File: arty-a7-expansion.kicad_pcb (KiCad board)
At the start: 4 copper layers, 109.2 x 47 mm, 121 parts, among them IC1 TPD8S009DSMR, IC2 PCA9500PW, J1 SJ-43516-SMT-GR, J2 1140084168, J3 SJ-43516-SMT-BE, J4 685119134923, J5 UE27AC54100, U1 TPS61232DRCT, U2 MAX3421EEHJ, U3 CS4344-CZZ, U4 CS5343-CZZ, U5 NC7SZ126P5X, Y1 ABM8G-12.000MHZ-18-D2Y-T

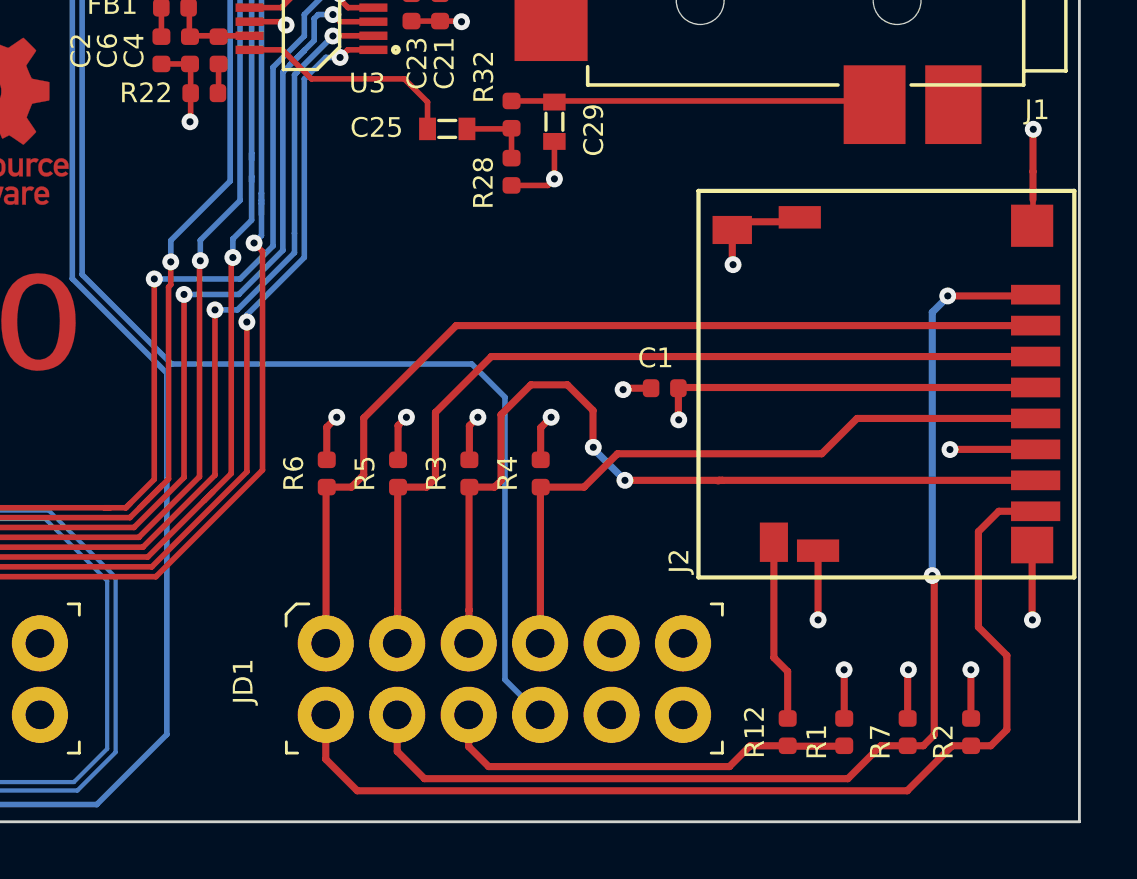
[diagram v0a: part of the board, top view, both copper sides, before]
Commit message: Replace micro SD card connector
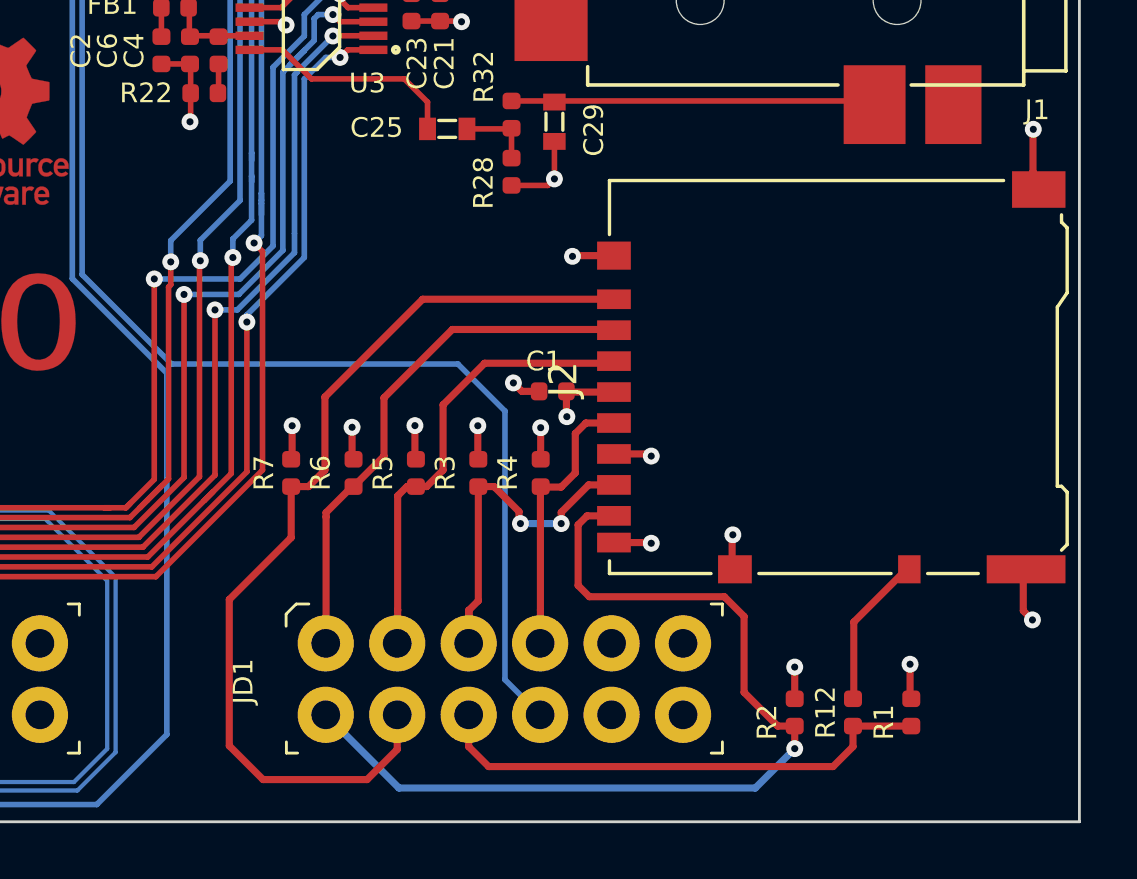
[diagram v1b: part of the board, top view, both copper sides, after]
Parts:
- D7: footprint antmicro-footprints:LED_0603 -> arty-a7-expansion-footprints:LED_0603
- J2: value 1140084168 -> DM3AT-SF-PEJM5; footprint arty-a7-expansion-footprints:MicroSD_1140084168 -> arty-a7-expansion-footprints:MicroSD_DM3AT-SF-PEJM5
- moved R7 23.8 mm to (181.6, 96.9)
- moved R2 6.31 mm to (199.5, 105.4)
- moved C1 3.98 mm to (190.9, 94.0)
- moved R1 2.48 mm to (203.6, 105.4)
- moved R12 2.42 mm to (201.6, 105.4)
- moved J2 1.97 mm to (200.8, 93.5)
- moved R6 0.95 mm to (183.8, 96.9)
- moved R5 0.64 mm to (186.0, 96.9)
- moved R3 0.32 mm to (188.2, 96.9)
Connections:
- J2 pad 10: GND -> Net-(J2-Pad10)
- J2 pad 9: Net-(J2-Pad9) -> GND
- R12 pad 2: Net-(J2-Pad9) -> Net-(J2-Pad10)
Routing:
- net /MISO_DAT0: track 31.0 -> 13.2 mm
- net /CD_DAT3: track 34.3 -> 18.8 mm
- net /MOSI_CMD: track 31.5 -> 16.2 mm
- net +3V3: track 68.0 -> 53.2 mm
- net /SCK: track 24.2 -> 9.85 mm
- net Net-(J2-Pad9): track 6.65 -> 0.00 mm
- net /DAT2: track 40.4 -> 33.9 mm, vias 2 -> 0
- net GND: track 105.4 -> 99.7 mm, vias 50 -> 51
- net Net-(J2-Pad10): track 0.00 -> 5.44 mm
- net /CD: track 15.8 -> 18.9 mm
- net /DAT1: track 37.0 -> 33.9 mm, vias 0 -> 1

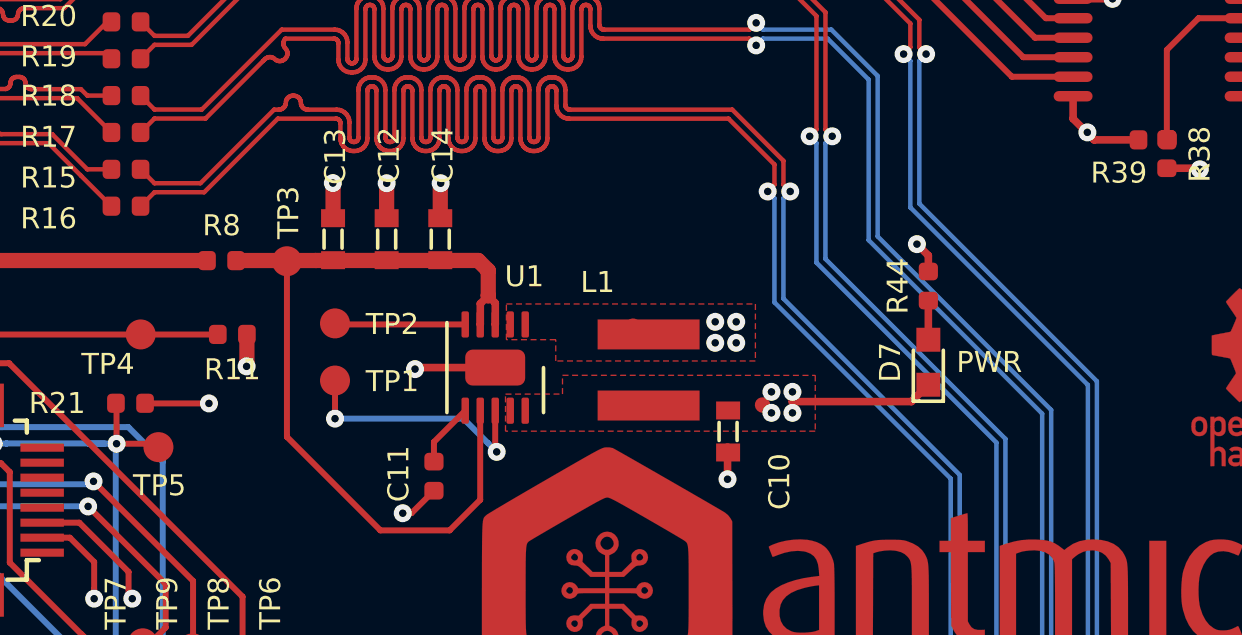
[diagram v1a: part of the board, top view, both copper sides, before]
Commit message: Add 5V0 led indicator
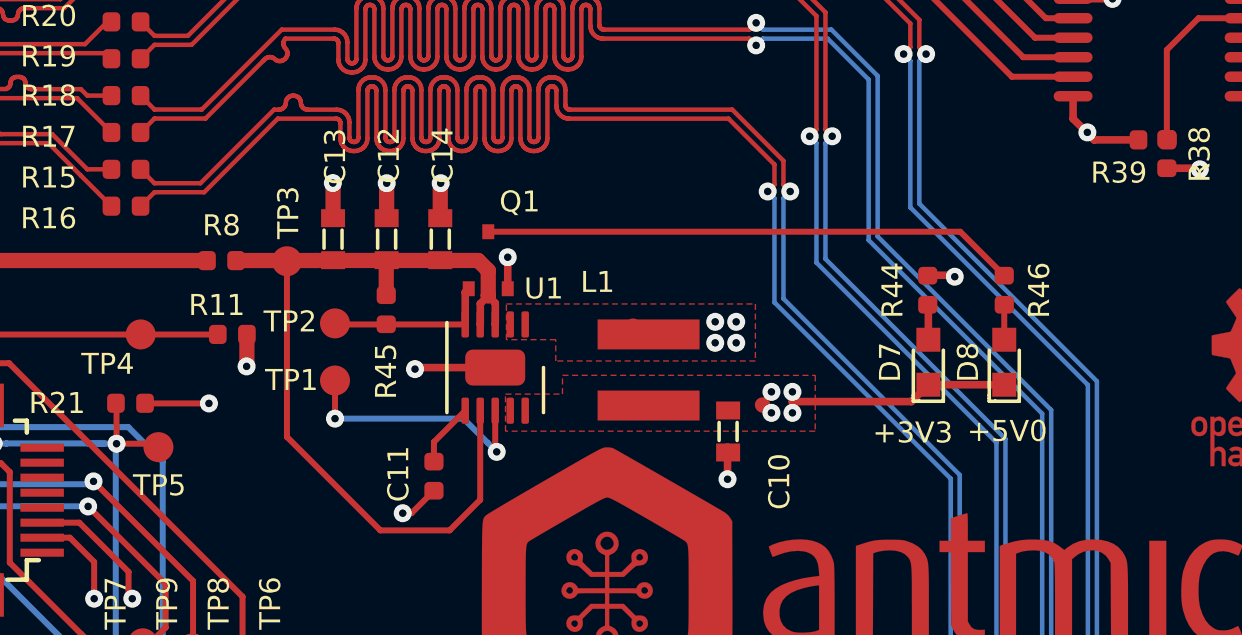
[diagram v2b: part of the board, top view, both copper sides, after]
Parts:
- added D8: LG_L29K-G2J1-24-Z, arty-a7-expansion-footprints:LED_0603, F.Cu at (161.3, 83.9)
- added Q1: BSS138APW, antmicro-footprints:SC70-3, F.Cu at (144.1, 80.5)
- added R45: R_10k_0402, antmicro-footprints:0402-res, F.Cu at (140.7, 82.1)
- added R46: R_330R_0402, antmicro-footprints:0402-res, F.Cu at (161.3, 81.5)
- R44: value R_100R_0402 -> R_330R_0402; footprint arty-a7-expansion-footprints:0402-res -> antmicro-footprints:0402-res
- moved R44 0.14 mm to (158.8, 81.5)
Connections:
- net Net-(C12-Pad1) renamed /5V0
- net Net-(TP2-Pad1) renamed /5V0_PG
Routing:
- net Net-(Q1-Pad3): track 0.00 -> 17.8 mm
- net +3V3: track 53.2 -> 55.8 mm
- net /5V0_PG: track 4.35 -> 5.59 mm
- net /5V0: track 28.5 -> 29.7 mm
- net Net-(D8-Pad2): track 0.00 -> 1.17 mm
- net GND: track 99.7 -> 100.6 mm, vias 51 -> 52
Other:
- board text added: "+3V3"
- board text added: "+5V0"
- board text removed: "PWR"

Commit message: Bump revision to 2.1.0
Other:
- board text added: "Rev.2.1.0 02/2021"
- board text removed: "Rev.2.0.1 07/2020"
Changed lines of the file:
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@@
-(kicad_pcb (version 20171130) (host pcbnew 5.1.6+dfsg1-1~bpo10+1)
+(kicad_pcb (version 20171130) (host pcbnew 5.1.5+dfsg1-2~bpo10+1)
   (general
     (thickness 1.6)
@@
   )
   (setup
-    (last_trace_width 0.508)
+    (last_trace_width 0.254)
     (user_trace_width 0.2)
     (user_trace_width 0.508)
@@
     (effects (font (size 1 1) (thickness 0.25)) (justify left))
   )
-  (gr_text "Rev.2.0.1 07/2020" (at 153.95 96.9385) (layer F.Mask)
+  (gr_text "Rev.2.1.0 02/2021" (at 153.95 96.9385) (layer F.Mask)
     (effects (font (size 1 1) (thickness 0.2)) (justify left))
   )
-  (gr_text "Rev.2.0.1 07/2020" (at 153.95 96.9385) (layer F.Cu)
+  (gr_text "Rev.2.1.0 02/2021" (at 153.95 96.9385) (layer F.Cu)
     (effects (font (size 1 1) (thickness 0.2)) (justify left))
   )
@@
   (segment (start 187.901241 101.773709) (end 187.911241 101.763709) (width 0.254) (layer F.Cu) (net 25))
   (segment (start 187.901241 102.943709) (end 187.901241 101.773709) (width 0.254) (layer F.Cu) (net 25))
-  (segment (start 137.431241 86.374711) (end 137.431241 80.495209) (width 0.2) (layer F.Cu) (net 124))
-  (segment (start 140.54724 89.49071) (end 137.431241 86.374711) (width 0.2) (layer F.Cu) (net 124))
-  (segment (start 142.85424 89.49071) (end 140.54724 89.49071) (width 0.2) (layer F.Cu) (net 124))
-  (segment (start 143.873241 85.501209) (end 143.873241 88.471709) (width 0.2) (layer F.Cu) (net 124))
-  (segment (start 143.873241 88.471709) (end 142.85424 89.49071) (width 0.2) (layer F.Cu) (net 124))
-  (segment (start 138.391241 80.493709) (end 143.806241 80.493709) (width 0.508) (layer F.Cu) (net 124))
-  (segment (start 137.431241 80.495209) (end 138.389741 80.495209) (width 0.508) (layer F.Cu) (net 124))
-  (segment (start 143.806241 80.493709) (end 144.141241 80.828709) (width 0.508) (layer F.Cu) (net 124))
-  (segment (start 138.389741 80.495209) (end 138.391241 80.493709) (width 0.508) (layer F.Cu) (net 124))
-  (segment (start 144.136241 81.673709) (end 144.376241 81.913709) (width 0.254) (layer F.Cu) (net 124))
-  (segment (start 143.876241 81.933709) (end 144.136241 81.673709) (width 0.254) (layer F.Cu) (net 124))
-  (segment (start 144.376241 81.913709) (end 144.376241 82.623209) (width 0.254) (layer F.Cu) (net 124))
-  (segment (start 143.873241 82.626209) (end 143.876241 82.623209) (width 0.254) (layer F.Cu) (net 124))
-  (segment (start 144.376241 82.623209) (end 144.373241 82.626209) (width 0.254) (layer F.Cu) (net 124))
-  (segment (start 143.876241 82.623209) (end 143.876241 81.933709) (width 0.254) (layer F.Cu) (net 124))
-  (segment (start 144.141241 81.668709) (end 144.136241 81.673709) (width 0.508) (layer F.Cu) (net 124))
-  (segment (start 144.141241 80.828709) (end 144.141241 81.668709) (width 0.508) (layer F.Cu) (net 124))
-  (segment (start 135.739741 80.495209) (end 137.431241 80.495209) (width 0.508) (layer F.Cu) (net 124))
-  (segment (start 135.736241 80.498709) (end 135.739741 80.495209) (width 0.508) (layer F.Cu) (net 124))
-  (segment (start 139.068741 82.626209) (end 139.033241 82.590709) (width 0.2) (layer F.Cu) (net 122))
-  (segment (start 143.373241 82.626209) (end 139.068741 82.626209) (width 0.2) (layer F.Cu) (net 122))
   (segment (start 142.331241 86.543209) (end 142.331241 87.198709) (width 0.2) (layer F.Cu) (net 26))
   (segment (start 143.373241 85.501209) (end 142.331241 86.543209) (width 0.2) (layer F.Cu) (net 26))
@@
   (segment (start 201.59124 104.76371) (end 201.59124 102.185693) (width 0.254) (layer F.Cu) (net 120))
   (segment (start 161.34124 83.135693) (end 161.34124 81.970693) (width 0.2) (layer F.Cu) (net 121))
+  (segment (start 139.068741 82.626209) (end 139.033241 82.590709) (width 0.2) (layer F.Cu) (net 122))
+  (segment (start 143.373241 82.626209) (end 139.068741 82.626209) (width 0.2) (layer F.Cu) (net 122))
   (segment (start 143.373241 81.553692) (end 143.49124 81.435693) (width 0.254) (layer F.Cu) (net 122))
   (segment (start 143.373241 82.626209) (end 143.373241 81.553692) (width 0.254) (layer F.Cu) (net 122))
   (segment (start 159.87624 79.535693) (end 161.34124 81.000693) (width 0.2) (layer F.Cu) (net 123))
   (segment (start 144.14124 79.535693) (end 159.87624 79.535693) (width 0.2) (layer F.Cu) (net 123))
+  (segment (start 137.431241 86.374711) (end 137.431241 80.495209) (width 0.2) (layer F.Cu) (net 124))
+  (segment (start 140.54724 89.49071) (end 137.431241 86.374711) (width 0.2) (layer F.Cu) (net 124))
+  (segment (start 142.85424 89.49071) (end 140.54724 89.49071) (width 0.2) (layer F.Cu) (net 124))
+  (segment (start 143.873241 85.501209) (end 143.873241 88.471709) (width 0.2) (layer F.Cu) (net 124))
+  (segment (start 143.873241 88.471709) (end 142.85424 89.49071) (width 0.2) (layer F.Cu) (net 124))
+  (segment (start 138.391241 80.493709) (end 143.806241 80.493709) (width 0.508) (layer F.Cu) (net 124))
+  (segment (start 137.431241 80.495209) (end 138.389741 80.495209) (width 0.508) (layer F.Cu) (net 124))
+  (segment (start 143.806241 80.493709) (end 144.141241 80.828709) (width 0.508) (layer F.Cu) (net 124))
+  (segment (start 138.389741 80.495209) (end 138.391241 80.493709) (width 0.508) (layer F.Cu) (net 124))
+  (segment (start 144.136241 81.673709) (end 144.376241 81.913709) (width 0.254) (layer F.Cu) (net 124))
+  (segment (start 143.876241 81.933709) (end 144.136241 81.673709) (width 0.254) (layer F.Cu) (net 124))
+  (segment (start 144.376241 81.913709) (end 144.376241 82.623209) (width 0.254) (layer F.Cu) (net 124))
+  (segment (start 143.873241 82.626209) (end 143.876241 82.623209) (width 0.254) (layer F.Cu) (net 124))
+  (segment (start 144.376241 82.623209) (end 144.373241 82.626209) (width 0.254) (layer F.Cu) (net 124))
+  (segment (start 143.876241 82.623209) (end 143.876241 81.933709) (width 0.254) (layer F.Cu) (net 124))
+  (segment (start 144.141241 81.668709) (end 144.136241 81.673709) (width 0.508) (layer F.Cu) (net 124))
+  (segment (start 144.141241 80.828709) (end 144.141241 81.668709) (width 0.508) (layer F.Cu) (net 124))
+  (segment (start 135.739741 80.495209) (end 137.431241 80.495209) (width 0.508) (layer F.Cu) (net 124))
+  (segment (start 135.736241 80.498709) (end 135.739741 80.495209) (width 0.508) (layer F.Cu) (net 124))
   (segment (start 140.74124 80.49721) (end 140.754741 80.483709) (width 0.508) (layer F.Cu) (net 124))
   (segment (start 140.74124 81.650693) (end 140.74124 80.49721) (width 0.508) (layer F.Cu) (net 124))
